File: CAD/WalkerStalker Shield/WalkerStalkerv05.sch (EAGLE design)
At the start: 25 parts

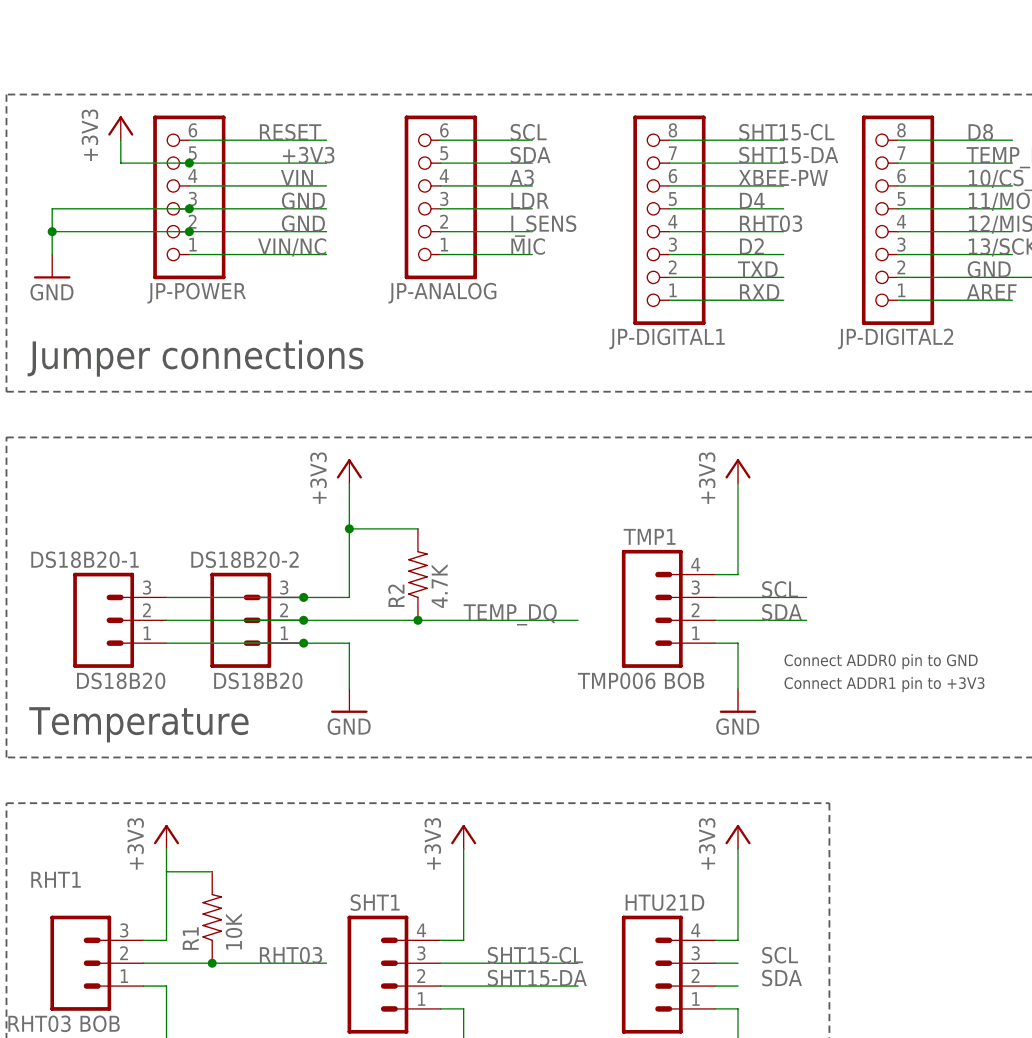
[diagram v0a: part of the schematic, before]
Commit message: Fixed Temperature sensors
+ Temperature sensors are now called by explicit address, rather than
index, which was not consistent (could not tell if sensor was wall or
air)
+ Unit IDs are not transmitted in data packets for easy identification
+Mounting bracket for TMP006 sensor added (3D file)
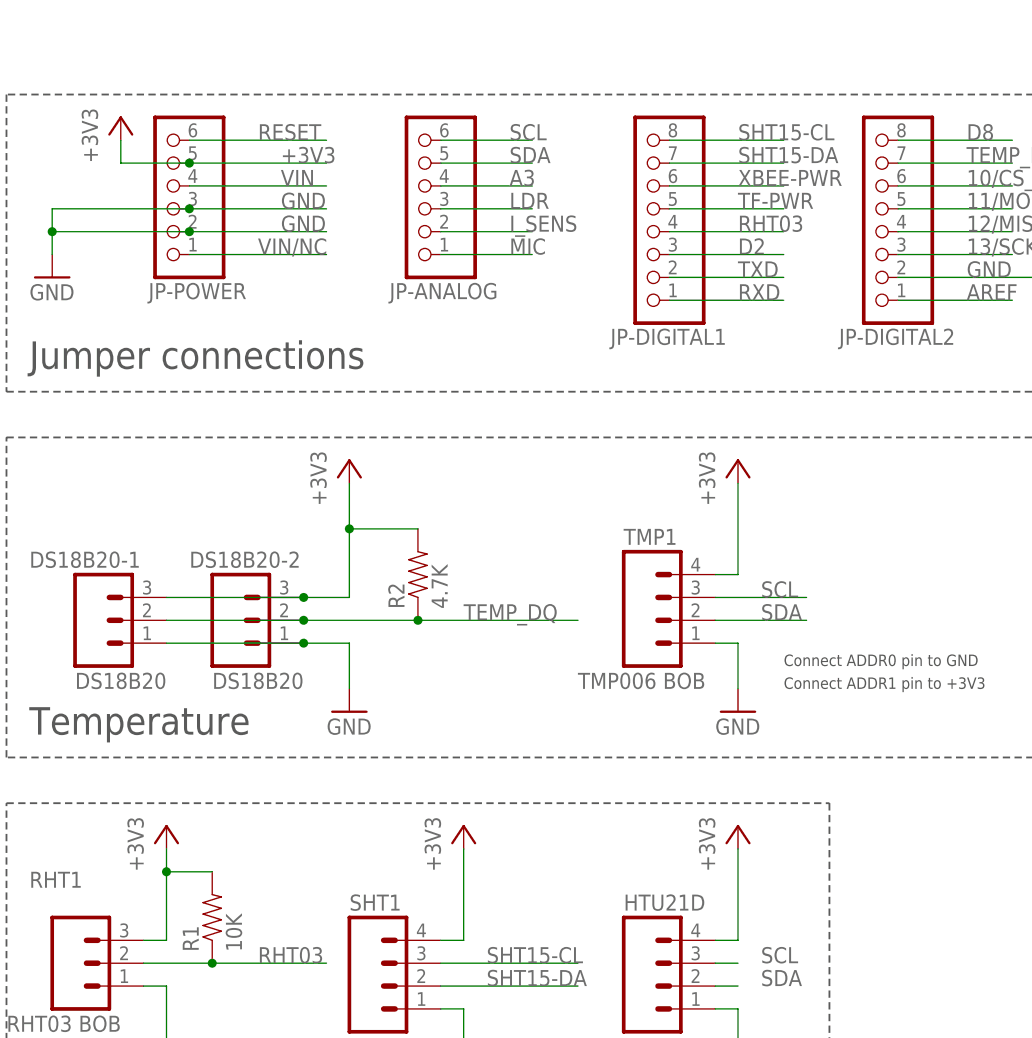
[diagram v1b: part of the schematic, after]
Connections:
- net D4 renamed TF-PWR
- net XBEE-PW renamed XBEE-PWR
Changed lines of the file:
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@@
 <?xml version="1.0" encoding="utf-8"?>
 <!DOCTYPE eagle SYSTEM "eagle.dtd">
-<eagle version="6.5.0">
+<eagle version="6.4">
 <drawing>
 <settings>
@@
 <pinref part="RHT1" gate="G$1" pin="3"/>
 <wire x1="25.4" y1="76.2" x2="27.94" y2="76.2" width="0.2032" layer="91"/>
+<junction x="27.94" y="83.82"/>
 </segment>
 <segment>
@@
 </segment>
 </net>
-<net name="D4" class="0">
+<net name="TF-PWR" class="0">
 <segment>
 <pinref part="JP-DIGITAL1" gate="A" pin="5"/>
@@
 </segment>
 </net>
-<net name="XBEE-PW" class="0">
+<net name="XBEE-PWR" class="0">
 <segment>
 <pinref part="JP-DIGITAL1" gate="A" pin="6"/>
